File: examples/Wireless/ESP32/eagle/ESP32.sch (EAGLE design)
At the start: 5 parts

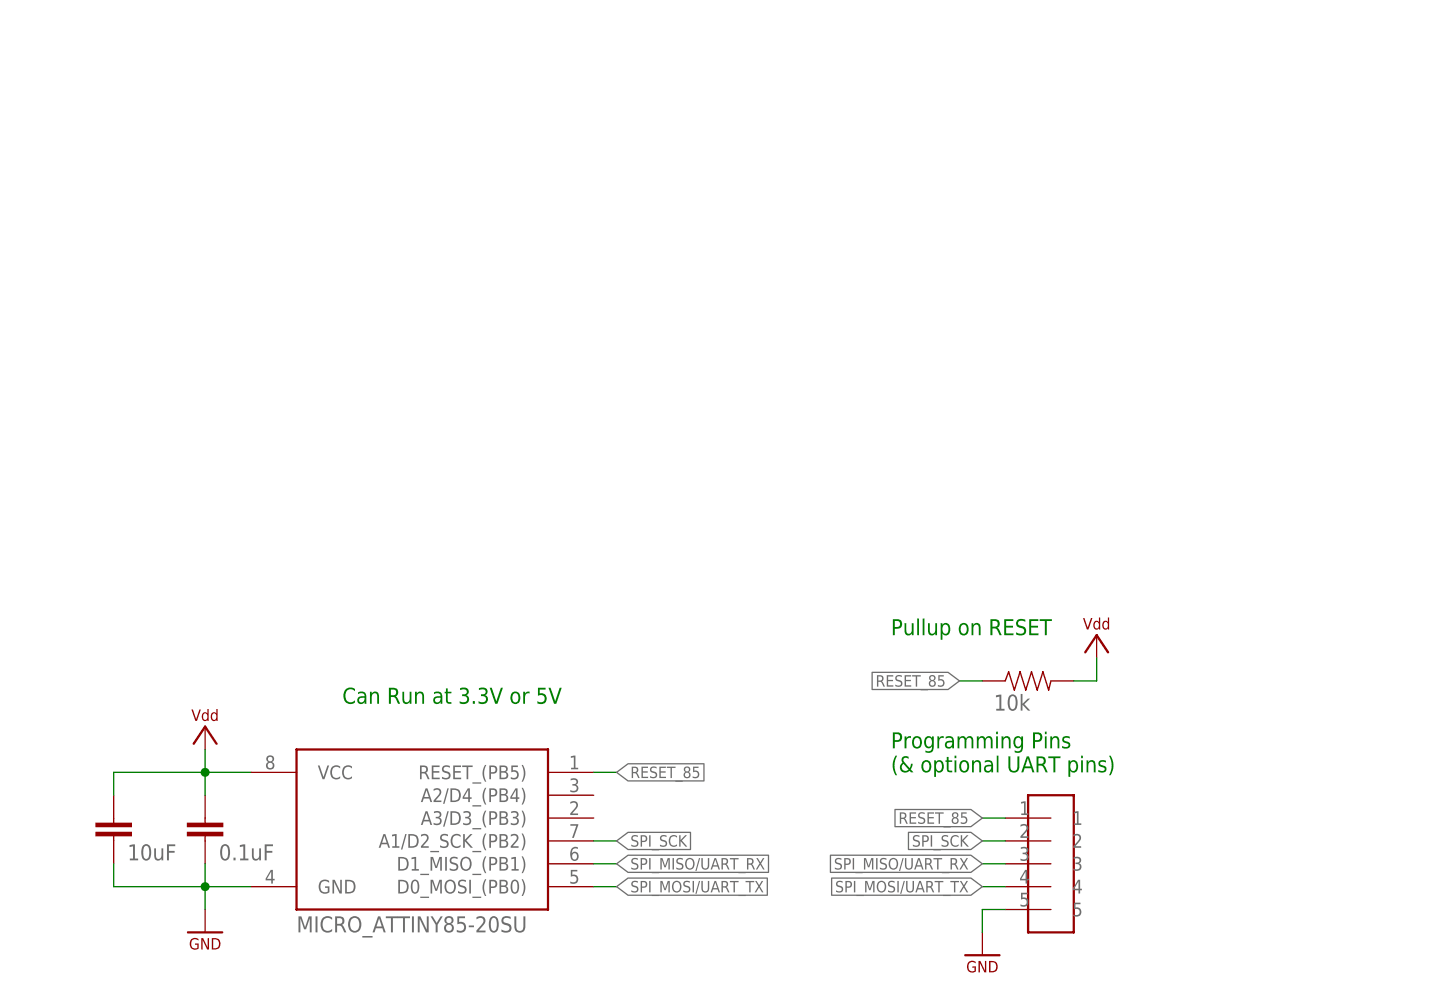
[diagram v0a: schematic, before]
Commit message: marquee template; schematic images
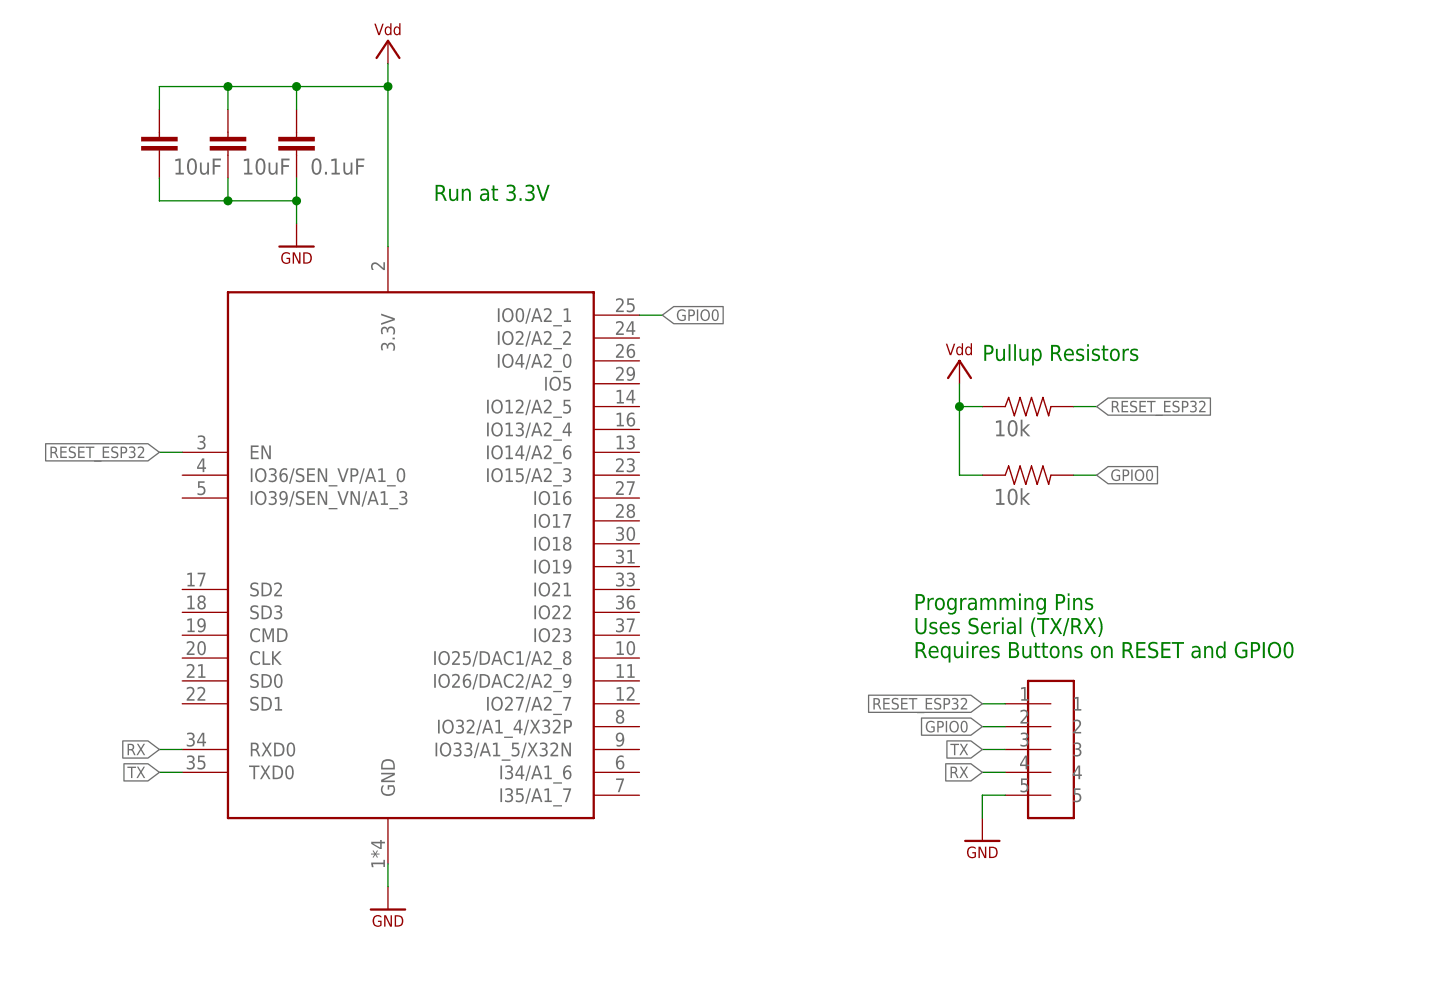
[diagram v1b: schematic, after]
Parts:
- removed U$2: HEADER-5-TESTPOINT, homemade-hardware:HEADER-5-TESTPOINT
- added C3: 10uF, homemade-hardware:COMPONENT_CAP-0805
- added R2: 10k, homemade-hardware:COMPONENT_RESISTOR-0805
- added X1: MICRO_ESP32, homemade-hardware:MICRO_ESP32
- U$1: value MICRO_ATTINY85-20SU -> HEADER-5-TESTPOINT; device homemade-hardware:MICRO_ATTINY85-20SU -> homemade-hardware:HEADER-5-TESTPOINT
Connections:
- removed net RESET_85: R1.1, U$1.RESET_(PB5), U$2.1
- removed net SPI_MISO/UART_RX: U$1.D1_MISO_(PB1), U$2.3
- removed net SPI_MOSI/UART_TX: U$1.D0_MOSI_(PB0), U$2.4
- removed net SPI_SCK: U$1.A1/D2_SCK_(PB2), U$2.2
- new net GPIO0: R2.2, U$1.2, X1.IO0/A2_1
- new net RESET_ESP32: R1.2, U$1.1, X1.EN
- new net RX: U$1.4, X1.RXD0
- new net TX: U$1.3, X1.TXD0
- net GND: now also C3.2, U$1.5, X1.GND; no longer U$1.GND, U$2.5
- net VDD: now also C3.1, R1.1, R2.1, X1.3.3V; no longer R1.2, U$1.VCC
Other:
- note added: "Programming Pins Uses Serial (TX/RX) Requires Buttons on RESET and GPIO0"
- note added: "Pullup Resistors"
- note added: "Run at 3.3V"
- note removed: "Can Run at 3.3V or 5V"
- note removed: "Programming Pins (& optional UART pins)"
- note removed: "Pullup on RESET"
